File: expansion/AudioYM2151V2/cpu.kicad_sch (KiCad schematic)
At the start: 31 parts, among them J3 JTAG_68K, J4 Serial Out, U10 74LS374, U11 74LS374, U12 68008, U13 74LS374, U14 74LS148, U15 AS6C4008-55PCN, U16 AT28C256B, U17 XC9536PC44, U18 SC26C92C1A, X2 8Mhz, Y1 3.6864Mhz

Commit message: Starting pcb layout
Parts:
- renumbered C42 to C39, C43 to C40, U12 to U10, U13 to U11, U14 to U12, U15 to U13, U16 to U14, U17 to U15, U18 to U16, U10 to U8, U11 to U9

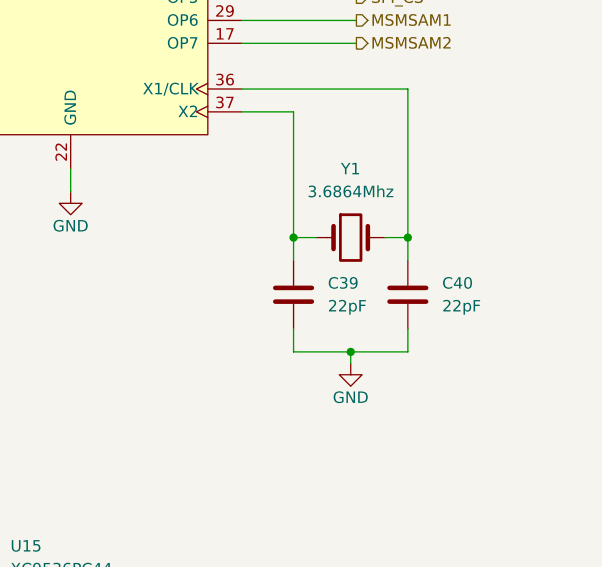
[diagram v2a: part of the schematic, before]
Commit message: Working on footprint positions
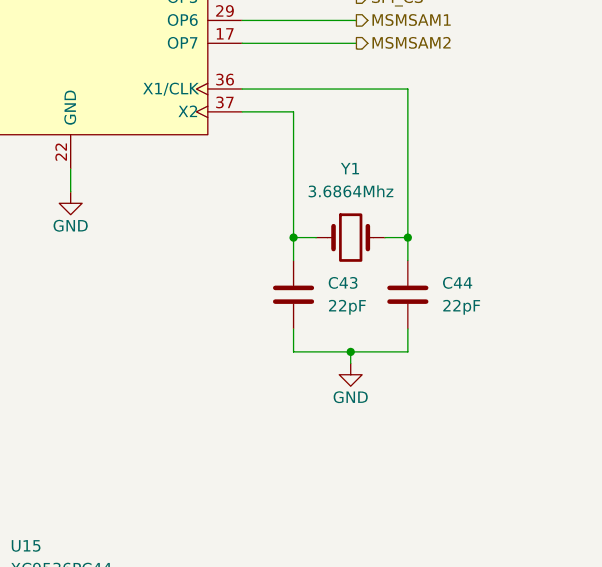
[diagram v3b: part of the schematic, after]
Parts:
- renumbered C39 to C43, C40 to C44

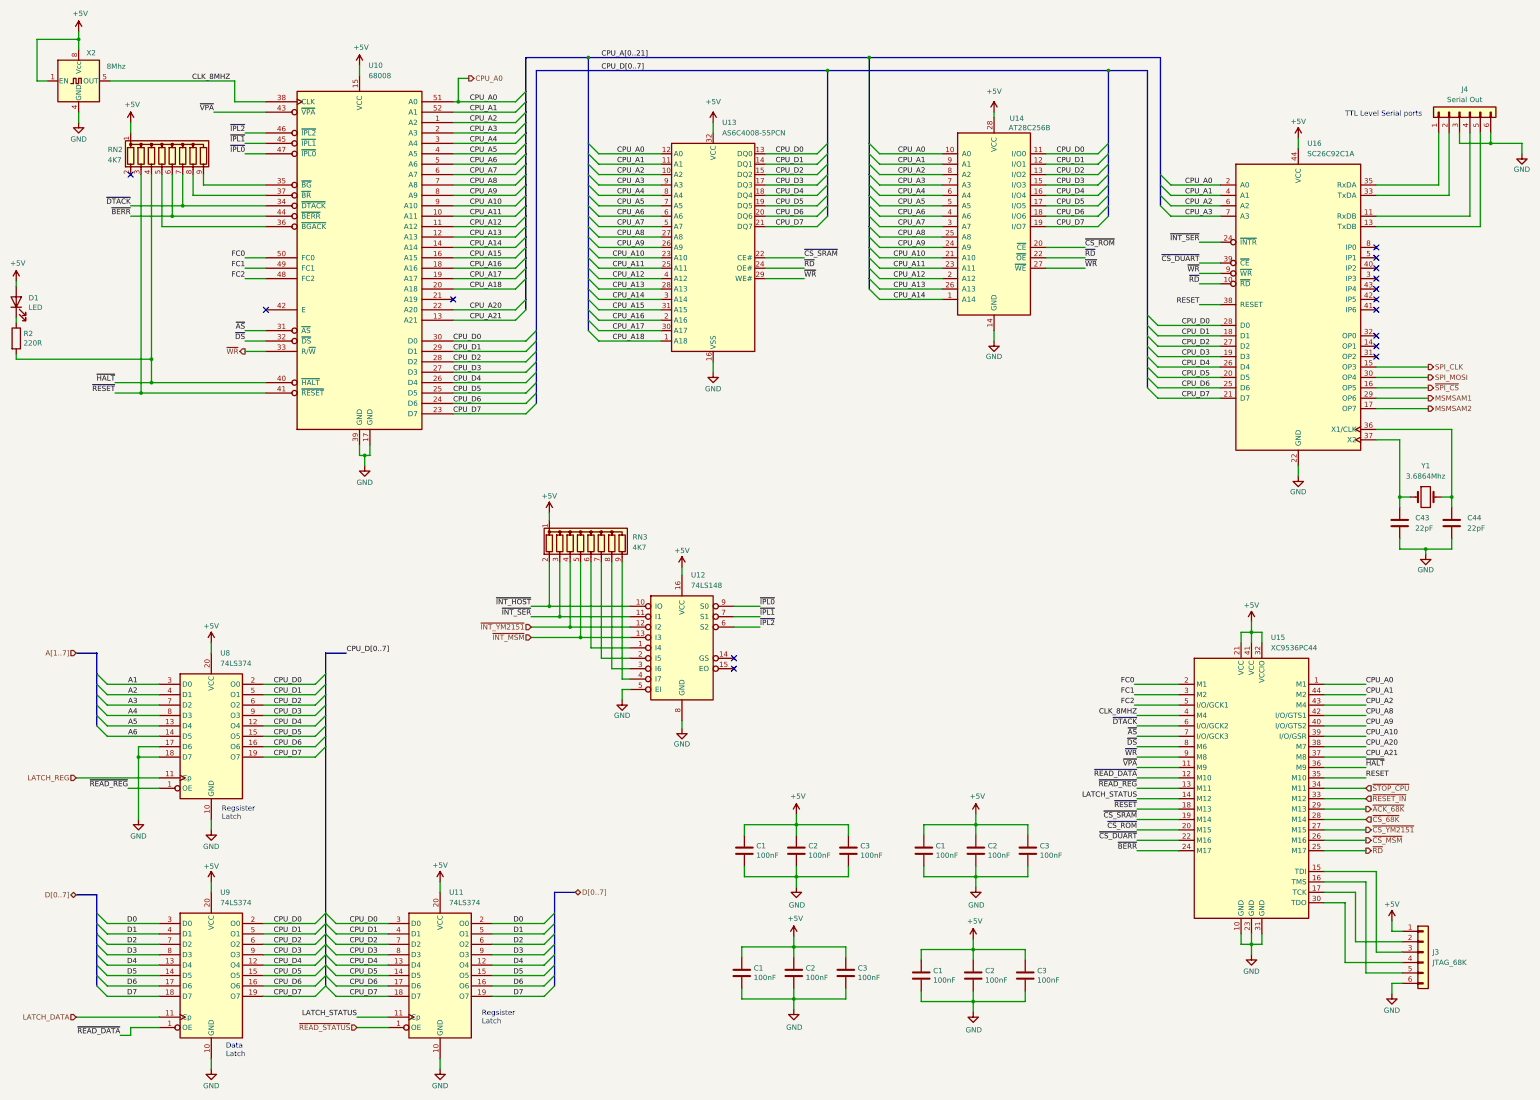
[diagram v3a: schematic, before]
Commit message: YM2151V2: added back second MSM chip
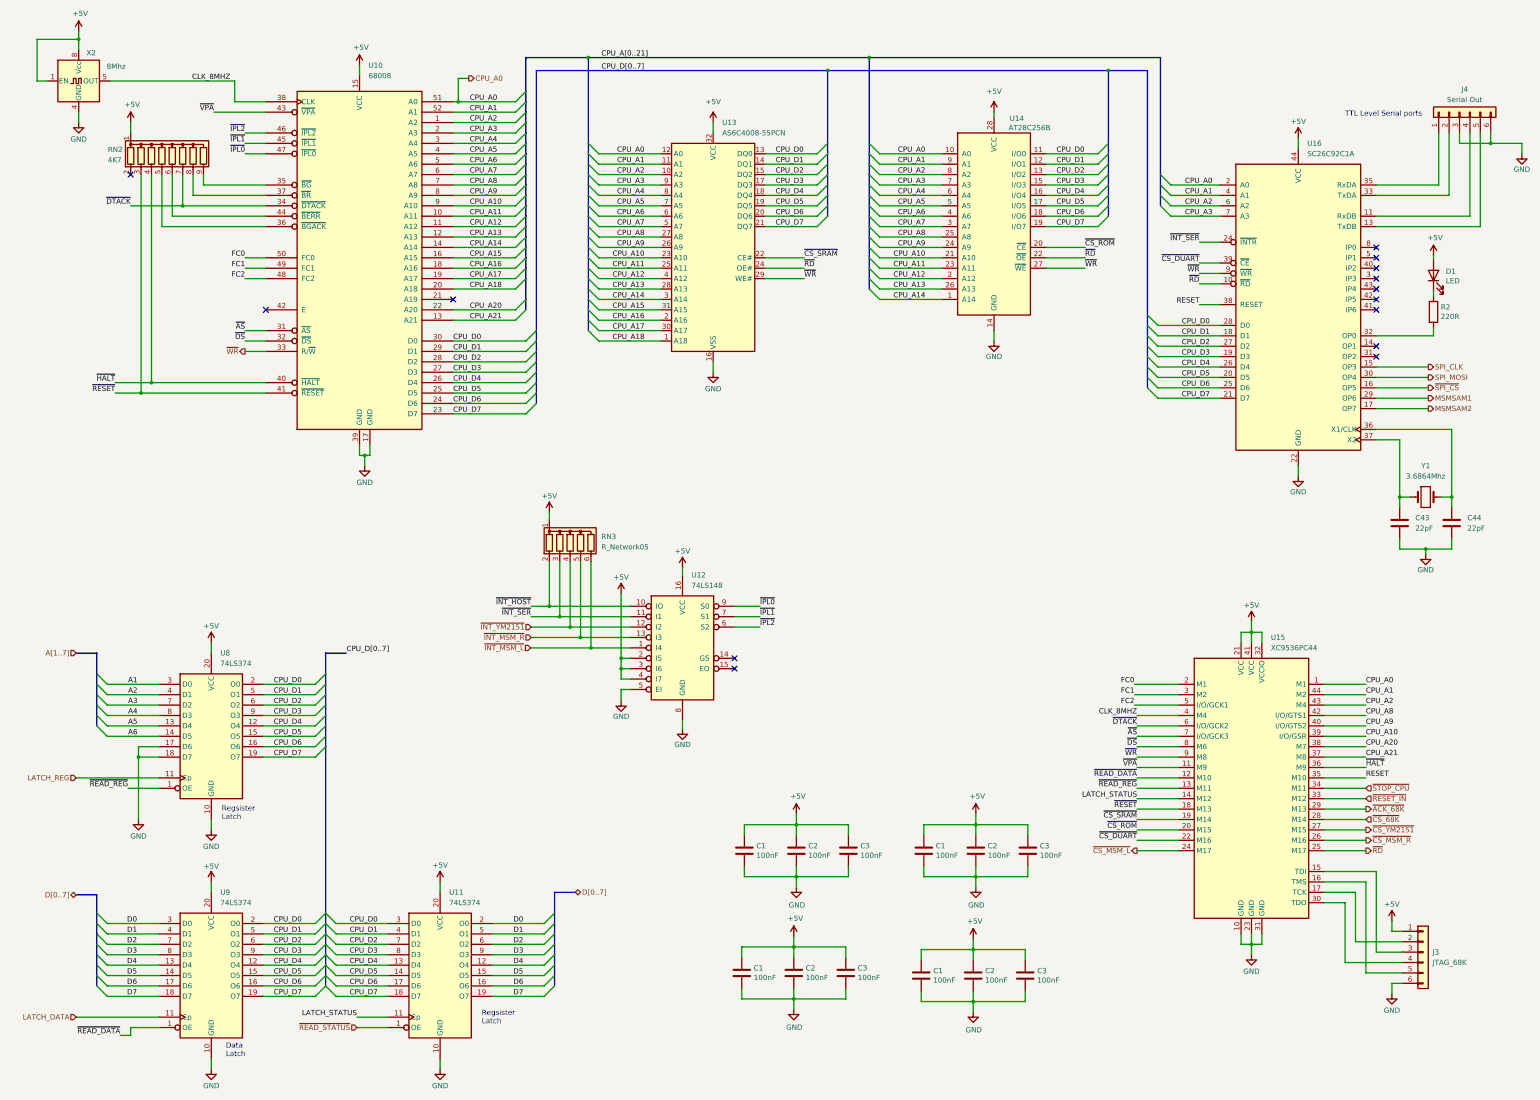
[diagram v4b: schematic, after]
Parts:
- removed RN3: 4K7, Resistor_THT:R_Array_SIP9, symbol Device:R_Network08
- added RN3: R_Network05, Resistor_THT:R_Array_SIP6, symbol Device:R_Network05
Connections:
- net +5V: now also U12.2 (I5), U12.3 (I6), U12.4 (I7), RN3.1 (common)
- net ~{HALT}: no longer R2.2
- net ~{INT_HOST}: now also RN3.2 (R1)
- net ~{INT_SER}: now also RN3.3 (R2)
- net ~{INT_YM2151}: now also RN3.4 (R3)
- net ~{INT_MSM_L}: now reaches U12.1 (I4)
- net ~{INT_MSM_L}: now also RN3.6 (R5)
- net at U16.32 (OP0): now also R2.2
- net ~{BERR}: no longer names the net of RN2.6 (R5), U10.44 (~{BERR})
- net ~{BERR}: no longer U15.24 (M17)
- net ~{CS_MSM} renamed ~{CS_MSM_R}
- net ~{INT_MSM} renamed ~{INT_MSM_R}
- net ~{INT_MSM_R}: now also RN3.5 (R4)
- new net ~{CS_MSM_L}: U15.24 (M17)
- no-connect marks 15 -> 14

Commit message: Finished YM2151 audio layout
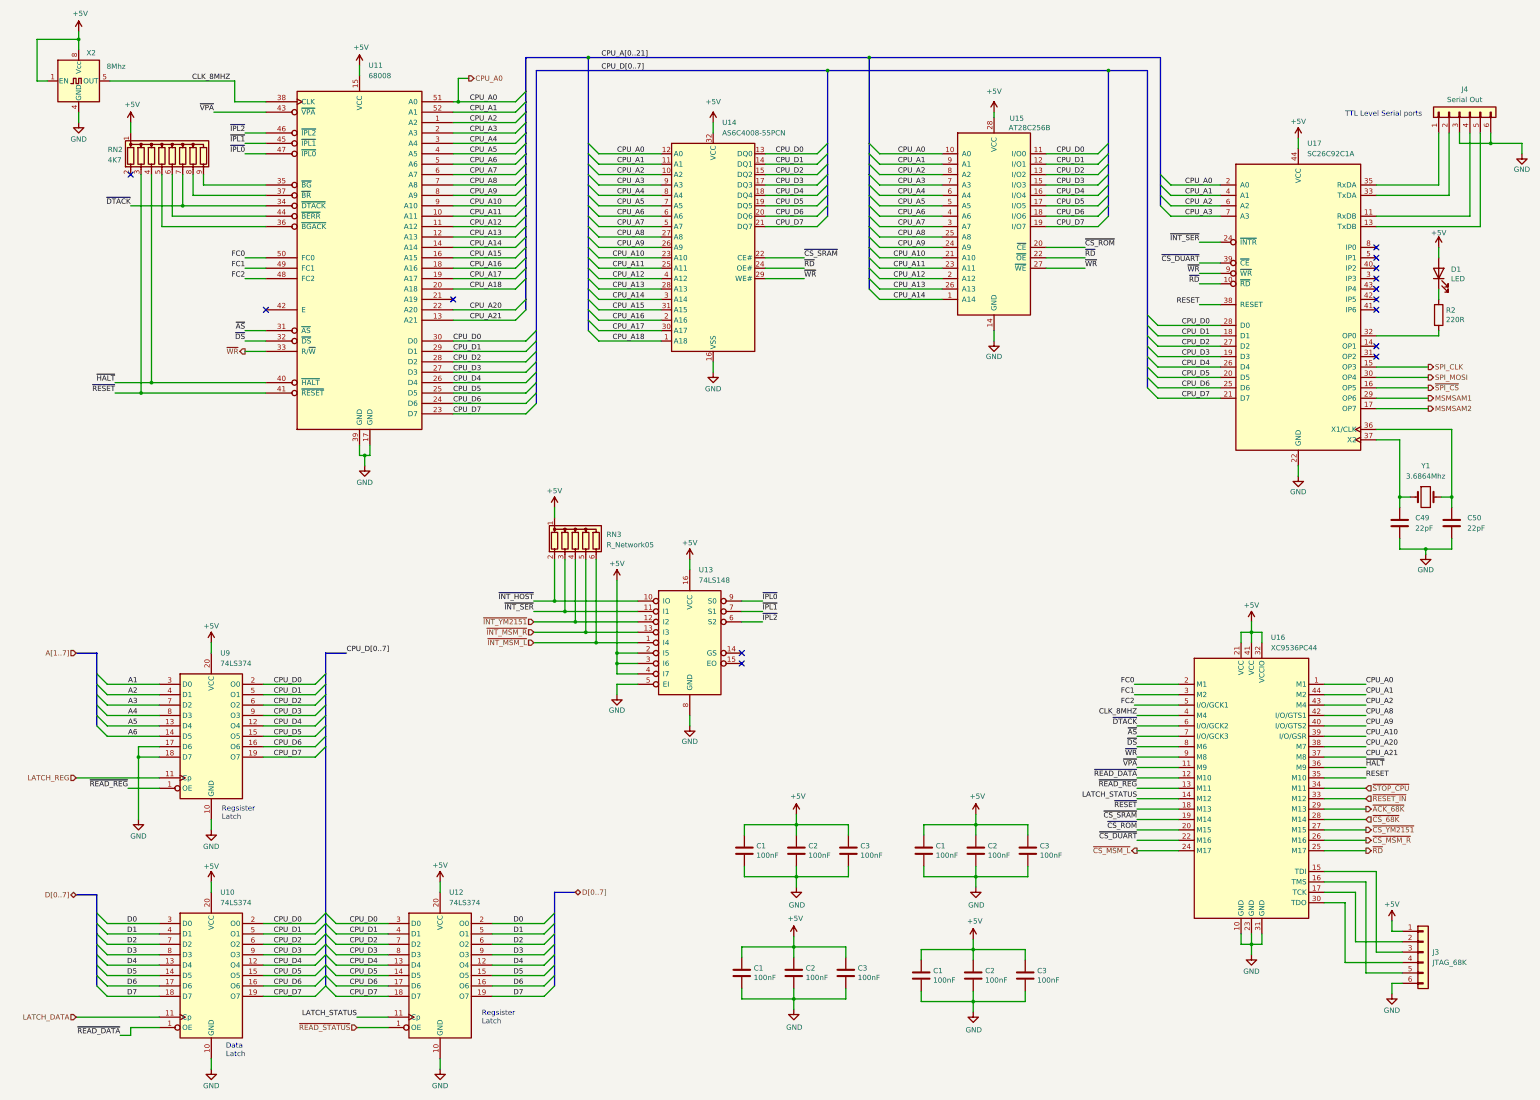
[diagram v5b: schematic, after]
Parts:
- renumbered C43 to C49, C44 to C50, U9 to U10, U10 to U11, U11 to U12, U12 to U13, U13 to U14, U14 to U15, U15 to U16, U16 to U17, U8 to U9
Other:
- moved on the sheet: D1, R2, RN3, U13
